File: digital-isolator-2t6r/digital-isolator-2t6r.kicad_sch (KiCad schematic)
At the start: 2 parts, among them J1 Conn_02x08_Odd_Even, J2 Conn_02x08_Odd_Even

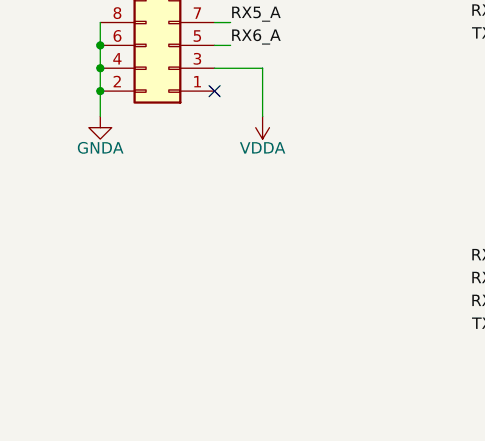
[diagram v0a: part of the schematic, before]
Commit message: Added copper tracks to digital iso 2t6r board for in-house fab
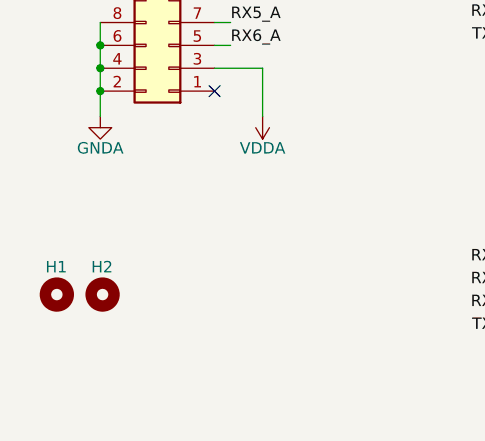
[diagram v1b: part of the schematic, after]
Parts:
- added H1, H2: MountingHole, MountingHole:MountingHole_3.2mm_M3, symbol Mechanical:MountingHole
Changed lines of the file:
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@@
     (pin "1")
+  )
+  (symbol (lib_id "Mechanical:MountingHole") (at 22.098 62.992 0) (unit 1)
+    (in_bom yes) (on_board yes)
+    (property "Reference" "H1" (id 0) (at 20.828 59.944 0)
+      (effects (font (size 1.27 1.27)) (justify left))
+    )
+    (property "Value" "MountingHole" (id 1) (at 24.892 64.2619 0)
+      (effects (font (size 1.27 1.27)) (justify left) hide)
+    )
+    (property "Footprint" "MountingHole:MountingHole_3.2mm_M3" (id 2) (at 22.098 62.992 0)
+      (effects (font (size 1.27 1.27)) hide)
+    )
+    (property "Datasheet" "~" (id 3) (at 22.098 62.992 0)
+      (effects (font (size 1.27 1.27)) hide)
+    )
   )
   (symbol (lib_id "CL_power:GNDB") (at 97.536 72.39 0) (unit 1)
@@
     )
     (pin "1")
+  )
+  (symbol (lib_id "Mechanical:MountingHole") (at 27.178 62.992 0) (unit 1)
+    (in_bom yes) (on_board yes)
+    (property "Reference" "H2" (id 0) (at 25.908 59.944 0)
+      (effects (font (size 1.27 1.27)) (justify left))
+    )
+    (property "Value" "MountingHole" (id 1) (at 29.972 64.2619 0)
+      (effects (font (size 1.27 1.27)) (justify left) hide)
+    )
+    (property "Footprint" "MountingHole:MountingHole_3.2mm_M3" (id 2) (at 27.178 62.992 0)
+      (effects (font (size 1.27 1.27)) hide)
+    )
+    (property "Datasheet" "~" (id 3) (at 27.178 62.992 0)
+      (effects (font (size 1.27 1.27)) hide)
+    )
   )
   (symbol (lib_id "power:VDDA") (at 73.66 22.352 0) (unit 1)
@@
       (reference "C8") (unit 1) (value "100nF") (footprint "Capacitor_SMD:C_0805_2012Metric_Pad1.18x1.45mm_HandSolder")
     )
+    (path "/28a92622-543c-40c5-bae8-ba1fb0fd5e57"
+      (reference "H1") (unit 1) (value "MountingHole") (footprint "MountingHole:MountingHole_3.2mm_M3")
+    )
+    (path "/3baca290-7445-4ca3-924f-6e8a5ac09b81"
+      (reference "H2") (unit 1) (value "MountingHole") (footprint "MountingHole:MountingHole_3.2mm_M3")
+    )
     (path "/097c6564-e2b6-465d-97a0-9593f820253f"
